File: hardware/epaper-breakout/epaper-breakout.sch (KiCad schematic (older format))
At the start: 68 parts, among them J1 XF2M-3315-1A, J2 C10418, J3 Conn_02x06_Counter_Clockwise, J4 ED060SC4, Q1 IRLML6402, U1 MCP1700-3302E_SOT23, U2 LT1945, U3 LT1945, U5 ESP32-WROVER, U6 CH330N, U7 LM358, U8 74HC4094-normal, U9 MCP9700AT-ETT

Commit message: v5: use ch340g with auto-reset
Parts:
- removed BOOT1: SW2, epaper-breakout:SW_TS-1187A, symbol Switch:SW_Push
- removed C16: 1nF, Capacitor_SMD:C_0603_1608Metric, symbol Device:C
- removed R11, R12: 470, Resistor_SMD:R_0805_2012Metric, symbol Device:R
- removed RESET1: SW1, epaper-breakout:SW_TS-1187A, symbol Switch:SW_Push
- removed U6: CH330N, Package_SO:SOIC-8_3.9x4.9mm_P1.27mm, symbol Interface_USB:CH330N
- added C?: 0.1uF, Capacitor_SMD:C_0603_1608Metric, symbol Device:C
- added Q? (x2): MBT3904DW1, Package_TO_SOT_SMD:SOT-363_SC-70-6, symbol Transistor_BJT:MBT3904DW1
- added R? (x2): 10k, Resistor_SMD:R_0805_2012Metric, symbol Device:R
- added U?: CH340G, Package_SO:SOIC-16_3.9x9.9mm_P1.27mm, symbol Interface_USB:CH340G
- added Y?: Crystal_GND2, symbol Device:Crystal_GND2
- C13, C14: value 0.1uF -> 10pF
- C15: value 1nF -> 0.1uF
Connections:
- net labels added: ~DTR, ~RTS
- wire segments 357 -> 373
- no-connect marks 19 -> 23
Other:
- note added: "Auto-Reset\n"
- moved on the sheet: C1, C10, C11, C12, C13, C14, C15, C19, C2, C20, C3, C4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

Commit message: xc5 connector, power management
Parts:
- removed Q1: IRLML6402, Package_TO_SOT_SMD:SOT-23, symbol Transistor_FET:IRLML6402
- removed Q? (x2): MBT3904DW1, Package_TO_SOT_SMD:SOT-363_SC-70-6, symbol Transistor_BJT:MBT3904DW1
- added Q1, Q2: AO3400A, Package_TO_SOT_SMD:SOT-23, symbol Transistor_FET:AO3400A
- added Q3, Q4: MMBT3904, Package_TO_SOT_SMD:SOT-23, symbol Transistor_BJT:MMBT3904
- added R12: 10k, Resistor_SMD:R_0805_2012Metric, symbol Device:R
- added U6: ED060XC5, epaper-breakout:X05A20H34G, symbol epd_breakout:ED060XC5
- gave numbers to parts that had none: 5
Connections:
- net labels added: EPD_VDD, SMPS_CTRL, SW_VIN
- net labels removed: EPD_POWER, EP_RL, ~SMPS_CTRL
- wire segments 373 -> 426

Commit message: WIP: partial routing
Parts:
- removed Q1, Q2: AO3400A, Package_TO_SOT_SMD:SOT-23, symbol Transistor_FET:AO3400A
- added Q1, Q6: MMBT3904, Package_TO_SOT_SMD:SOT-23, symbol Transistor_BJT:MMBT3904
- added Q2, Q5: AO3401A, Package_TO_SOT_SMD:SOT-23, symbol Transistor_FET:AO3401A
- added R20, R21: 10k, Resistor_SMD:R_0805_2012Metric, symbol Device:R
- added U10: ED060SC7, epaper-breakout:AXT334124, symbol epd_breakout:ED060SC7
- Q3, Q4: LCSC (none) -> C20526
- R12: value 10k -> 1k
- U4: LCSC (none) -> C14267
- Y1: footprint (none) -> Crystal:Crystal_SMD_3225-4Pin_3.2x2.5mm_HandSoldering; LCSC (none) -> C9002
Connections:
- wire segments 426 -> 463
- no-connect marks 23 -> 27
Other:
- moved on the sheet: H1, H2, H3, J1, J3, U9

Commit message: partial routing
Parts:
- removed Q1: MMBT3904, Package_TO_SOT_SMD:SOT-23, symbol Transistor_BJT:MMBT3904
- removed R2, R21, R3, R8, R9: 10k, Resistor_SMD:R_0805_2012Metric, symbol Device:R
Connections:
- net +3.3V: now also R15.1; no longer R15.2
- net EP_CKH: now also U5.23 (IO15); no longer U5.29 (IO5)
- net EP_CKV: now also U5.11 (IO26); no longer U5.10 (IO25)
- net EP_D0: now also Q4.3 (C), R15.2, U5.25 (IO0); no longer U5.9 (IO33_XTAL_32K_N)
- net EP_D1: now also U5.26 (IO4); no longer U5.8 (IO32_XTAL_32K_P)
- net EP_D2: now also U5.29 (IO5); no longer U5.26 (IO4)
- net EP_D3: now also U5.30 (IO18); no longer Q4.3 (C), R15.1, U5.25 (IO0)
- net EP_D4: now also U5.31 (IO19); no longer R13.1, U5.24 (IO2)
- net EP_D5: now also U5.33 (IO21); no longer U5.12 (IO27)
- net EP_D6: now also U5.36 (IO22); no longer U5.33 (IO21)
- net EP_D7: now also U5.37 (IO23); no longer U5.36 (IO22)
- net EP_LE: now also R13.1, U5.24 (IO2); no longer U5.23 (IO15)
- net EP_STH: now also U5.12 (IO27); no longer U5.11 (IO26)
- net at U8.3 (CP): now also U5.8 (IO32_XTAL_32K_P); no longer U5.30 (IO18)
- net at U8.1 (STROBE): now also U5.10 (IO25); no longer U5.31 (IO19)
- net at U8.2 (DATA): now also U5.9 (IO33_XTAL_32K_N); no longer U5.37 (IO23)
- net at Q2.1 (G), Q6.3 (C), R20.1: now also Q5.1 (G)
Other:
- moved on the sheet: Q5, Q6, R12, R15, U8

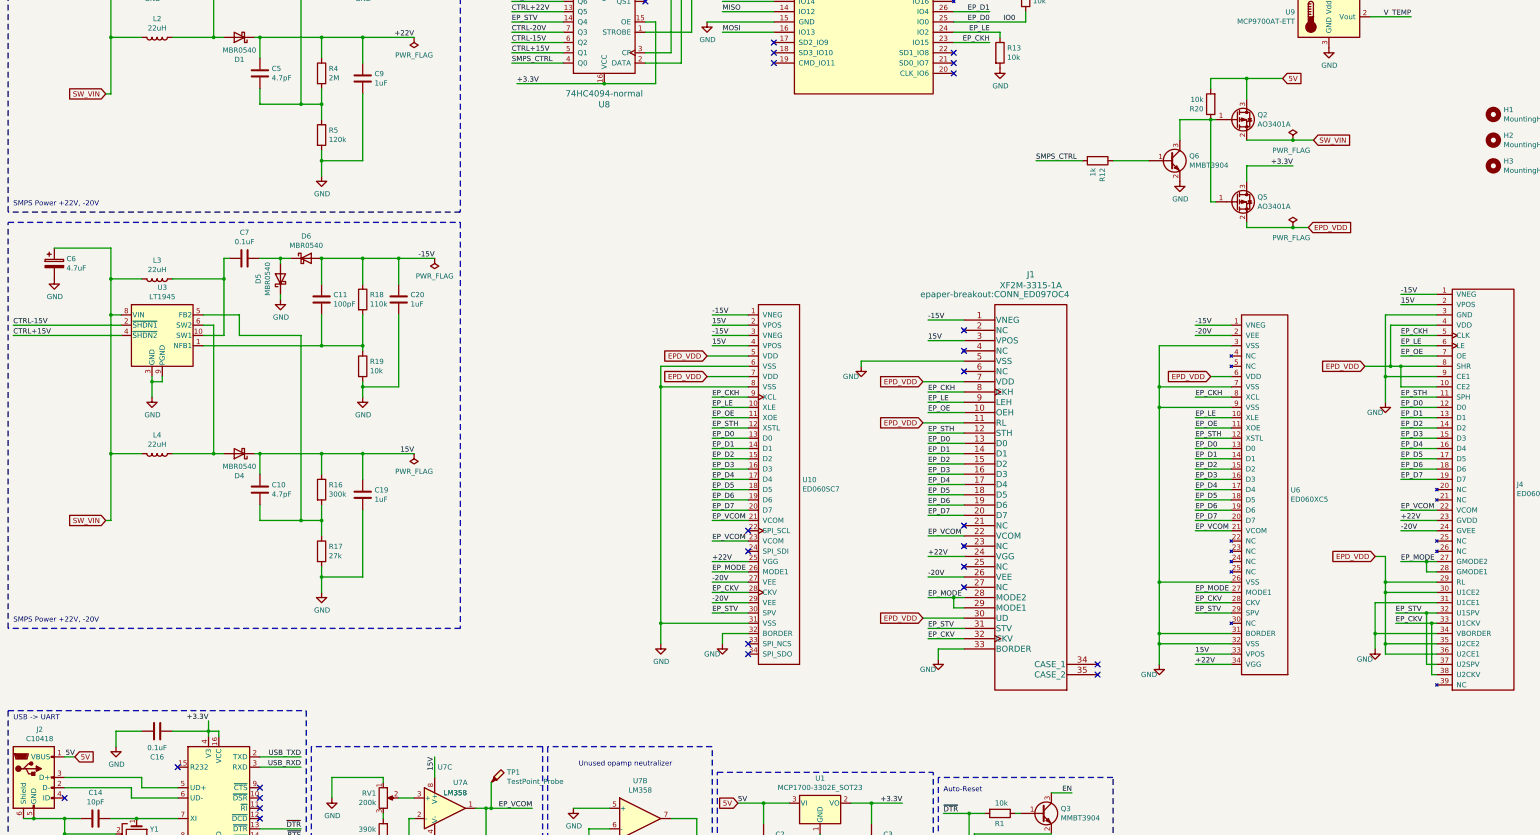
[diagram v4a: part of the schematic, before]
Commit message: v5: lipo charger circuit
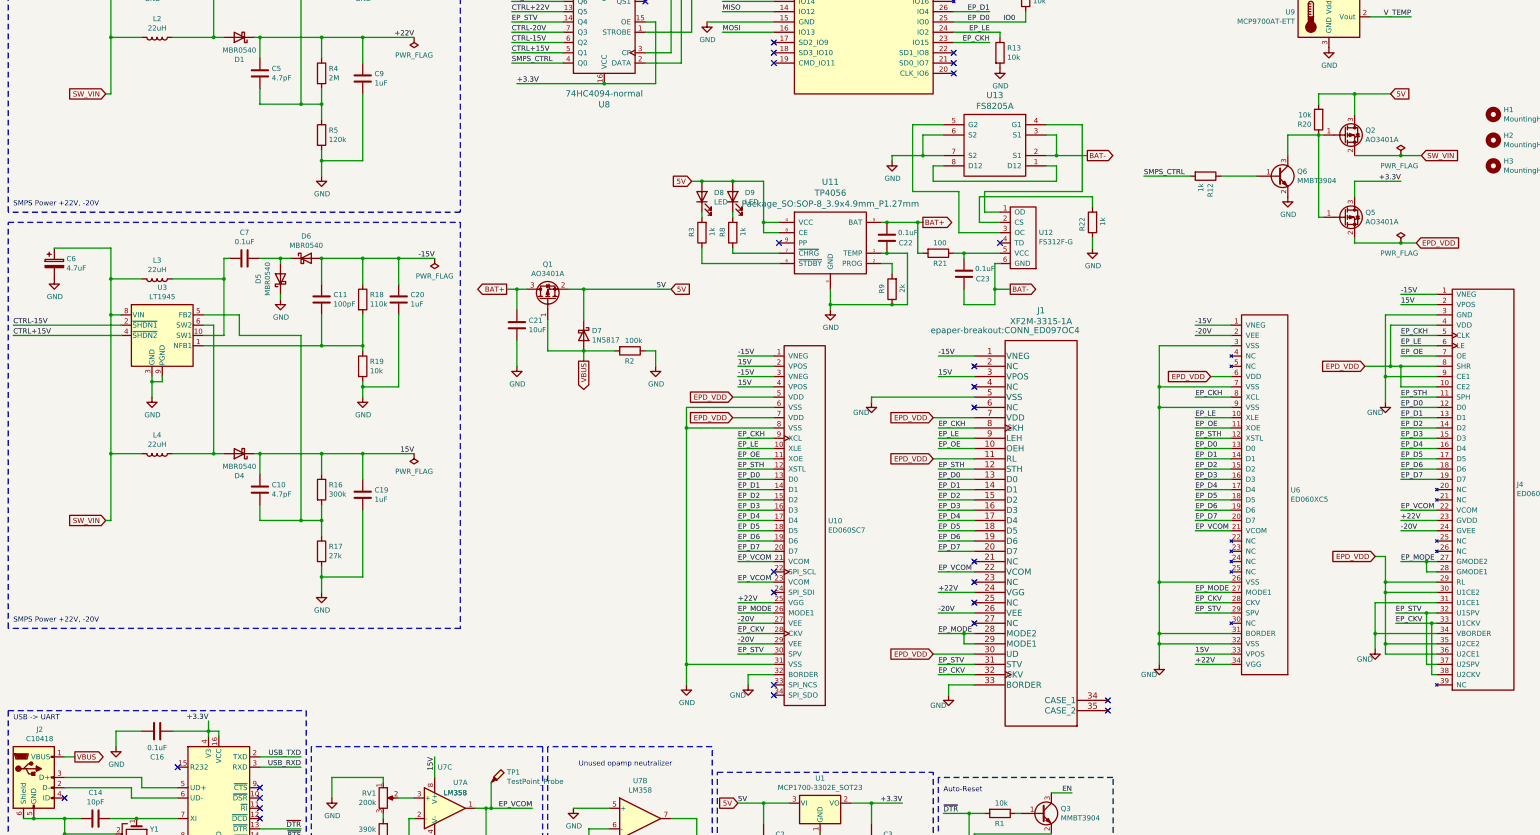
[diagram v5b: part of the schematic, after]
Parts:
- added C21: 10uF, Capacitor_SMD:C_0603_1608Metric, symbol Device:C
- added C22, C23: 0.1uF, Capacitor_SMD:C_0603_1608Metric, symbol Device:C
- added D7: 1N5817, Diode_THT:D_DO-41_SOD81_P10.16mm_Horizontal, symbol Diode:1N5817
- added D8, D9: LED, symbol Device:LED
- added Q1: AO3401A, Package_TO_SOT_SMD:SOT-23, symbol Transistor_FET:AO3401A
- added R2: 100k, Resistor_SMD:R_0805_2012Metric, symbol Device:R
- added R21: 100, Resistor_SMD:R_0805_2012Metric, symbol Device:R
- added R22, R3, R8: 1k, Resistor_SMD:R_0805_2012Metric, symbol Device:R
- added R9: 2k, Resistor_SMD:R_0805_2012Metric, symbol Device:R
- added U11: TP4056, Package_SO:SOP-8_3.9x4.9mm_P1.27mm, symbol tp4056:TP4056
- added U12: FS312F-G, Package_TO_SOT_SMD:SOT-23-6, symbol epd_breakout:FS312F-G
- added U13: FS8205A, Package_SO:TSSOP-8_4.4x3mm_P0.65mm, symbol fs8205a:FS8205A
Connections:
- net 5V: now also D7.1 (K), D8.2 (A), D9.2 (A), Q1.2 (S), U11.4 (VCC), U11.8 (CE); no longer J2.1 (VBUS)
- net GND: now also C21.2, C22.1, R2.1, R22.1, R9.1, U11.1 (TEMP), U11.3 (GND), U13.6 (S2), U13.7 (S2)
- new net: R8.1, U11.7 (~CHRG)
- new net: D9.1 (K), R8.2
- new net: R9.2, U11.2 (PROG)
- new net: R3.1, U11.6 (~STDBY)
- new net: U13.1 (D12), U13.8 (D12)
- new net: U12.1 (OD), U13.4 (G1)
- new net: U12.3 (OC), U13.5 (G2)
- new net: D8.1 (K), R3.2
- new net: R22.2, U12.2 (CS)
- new net: C23.2, R21.1, U12.5 (VCC)
- new net BAT+: C21.1, C22.2, Q1.3 (D), R21.2, U11.5 (BAT)
- new net BAT-: C23.1, U12.6 (GND), U13.2 (S1), U13.3 (S1)
- new net VBUS: D7.2 (A), J2.1 (VBUS), Q1.1 (G), R2.2
- no-connect marks 27 -> 29
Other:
- moved on the sheet: J1, Q2, Q5, Q6, R12, R20, U10

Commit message: v5 fix pin functions
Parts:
- D8: value LED -> LED GREEN; footprint (none) -> LED_SMD:LED_0805_2012Metric
- D9: value LED -> LED RED; footprint (none) -> LED_SMD:LED_0805_2012Metric
- U11: footprint Package_SO:SOP-8_3.9x4.9mm_P1.27mm -> epaper-breakout:TP4056_SOP-8-PP
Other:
- moved on the sheet: J1, J4, U10, U6

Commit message: more routing
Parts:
- added J?: Conn_01x02_Male, Connector_PinHeader_2.54mm:PinHeader_1x02_P2.54mm_Vertical, symbol Connector:Conn_01x02_Male
- D7: footprint Diode_THT:D_DO-41_SOD81_P10.16mm_Horizontal -> Diode_SMD:D_SOD-123
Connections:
- net BAT+: now also J?.1 (Pin_1)
- net BAT-: now also J?.2 (Pin_2)
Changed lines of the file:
@@
 F 0 "D7" V 6104 5830 50  0000 L CNN
 F 1 "1N5817" V 6195 5830 50  0000 L CNN
-F 2 "Diode_THT:D_DO-41_SOD81_P10.16mm_Horizontal" H 6150 5575 50  0001 C CNN
+F 2 "Diode_SMD:D_SOD-123" H 6150 5575 50  0001 C CNN
 F 3 "http://www.vishay.com/docs/88525/1n5817.pdf" H 6150 5750 50  0001 C CNN
 	1    6150 5750
@@
 Wire Wire Line
 	7600 4250 7900 4250
+$Comp
+L Connector:Conn_01x02_Male J?
+U 1 1 655CB8A7
+P 5750 6750
+F 0 "J?" H 5858 6931 50  0000 C CNN
+F 1 "Conn_01x02_Male" H 5858 6840 50  0000 C CNN
+F 2 "Connector_PinHeader_2.54mm:PinHeader_1x02_P2.54mm_Vertical" H 5750 6750 50  0001 C CNN
+F 3 "~" H 5750 6750 50  0001 C CNN
+	1    5750 6750
+	1    0    0    -1
+$EndComp
+Text GLabel 6100 6750 2    50   Input ~ 0
+BAT+
+Text GLabel 6100 6850 2    50   Input ~ 0
+BAT-
+Wire Wire Line
+	5950 6750 6100 6750
+Wire Wire Line
+	6100 6850 5950 6850
 $EndSCHEMATC

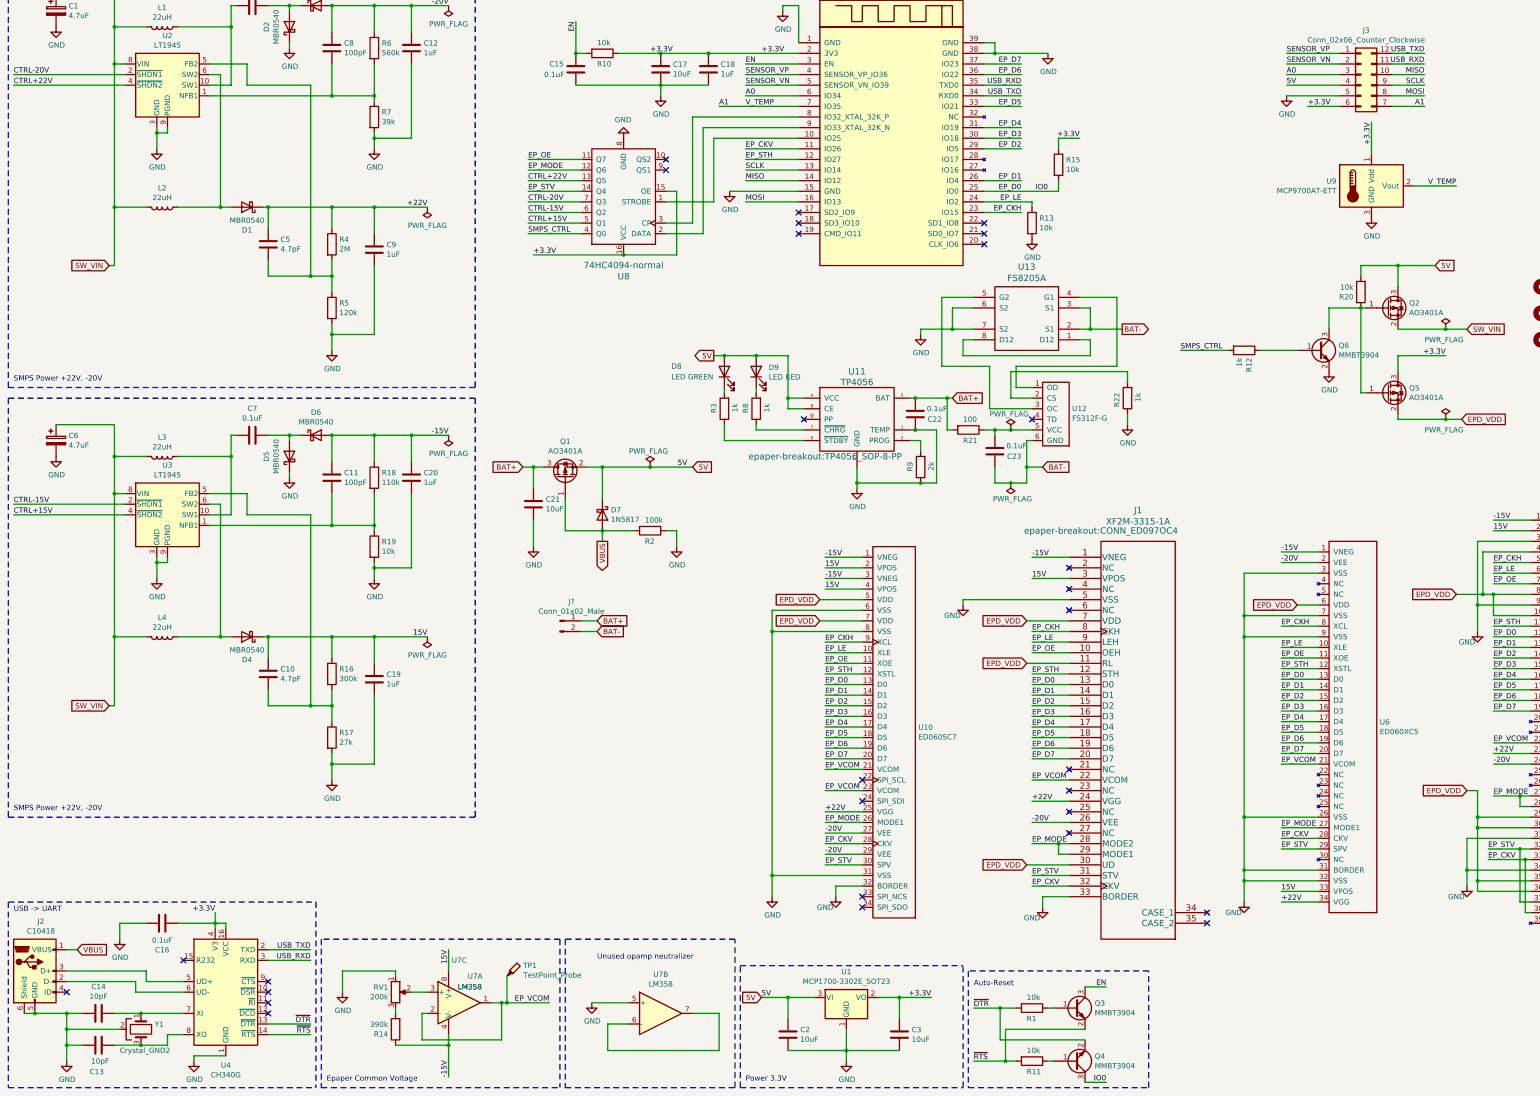
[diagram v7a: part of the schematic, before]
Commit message: remove battery protection, simplify
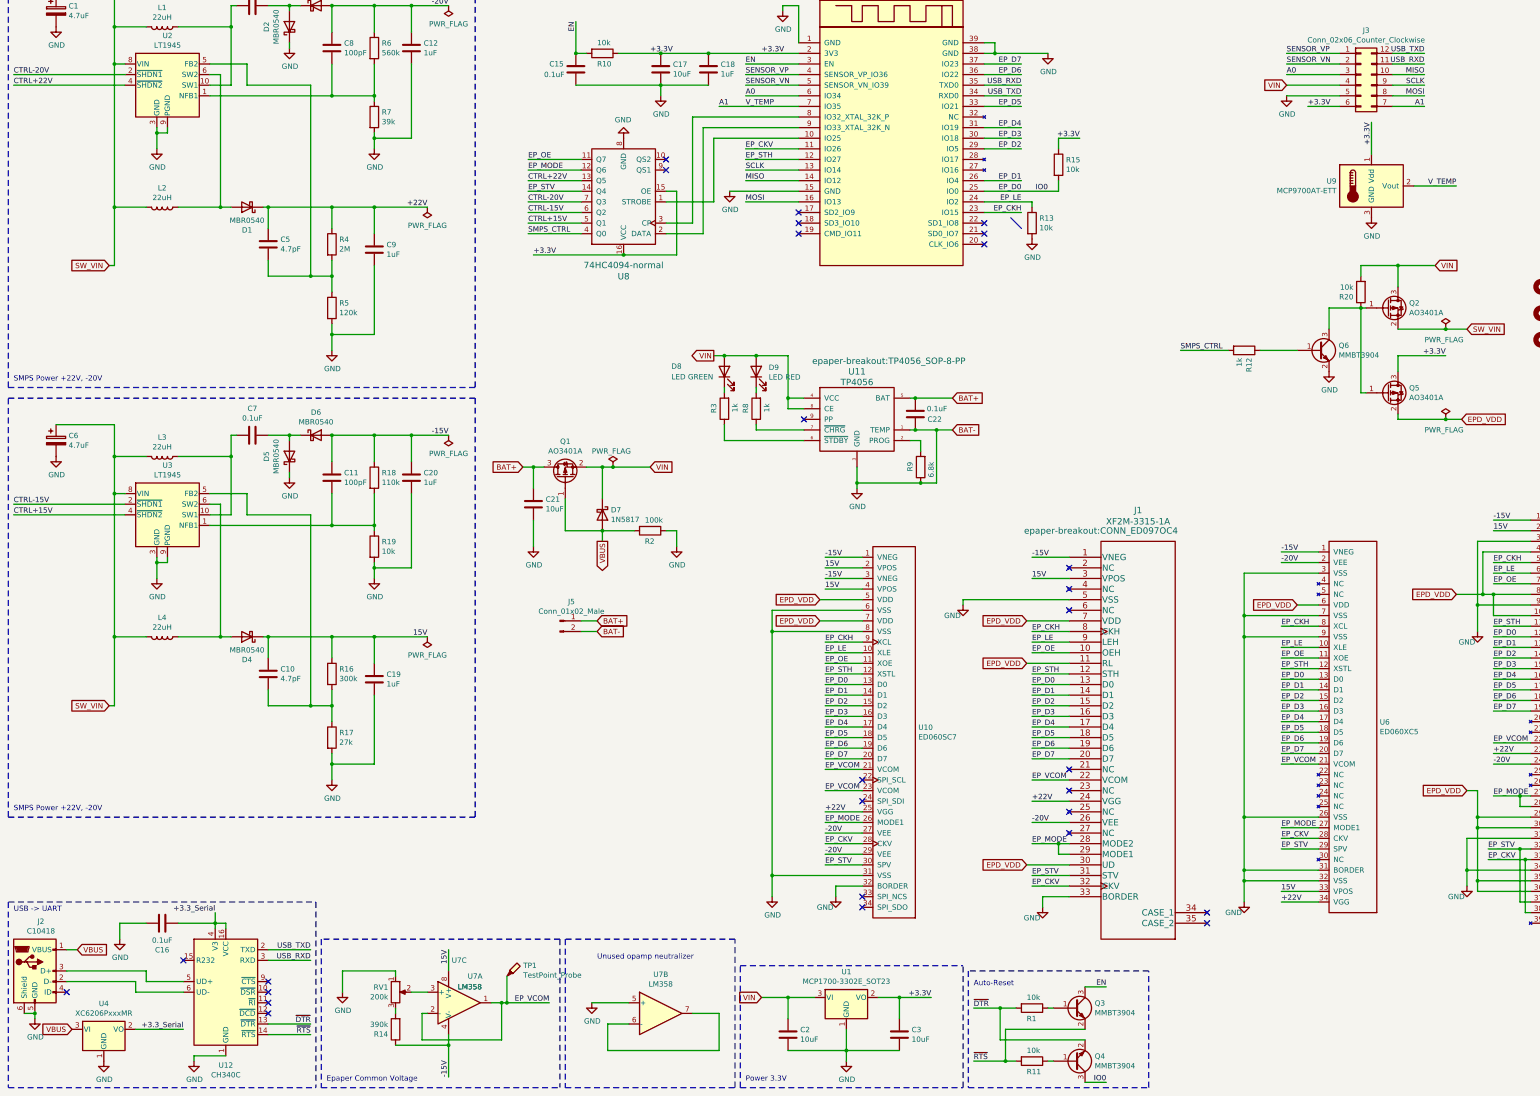
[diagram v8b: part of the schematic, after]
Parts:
- removed C13, C14: 10pF, Capacitor_SMD:C_0603_1608Metric, symbol Device:C
- removed C23: 0.1uF, Capacitor_SMD:C_0603_1608Metric, symbol Device:C
- removed R21: 100, Resistor_SMD:R_0805_2012Metric, symbol Device:R
- removed R22: 1k, Resistor_SMD:R_0805_2012Metric, symbol Device:R
- removed U12: FS312F-G, Package_TO_SOT_SMD:SOT-23-6, symbol epd_breakout:FS312F-G
- removed U13: FS8205A, Package_SO:TSSOP-8_4.4x3mm_P0.65mm, symbol fs8205a:FS8205A
- removed U4: CH340G, Package_SO:SOIC-16_3.9x9.9mm_P1.27mm, symbol Interface_USB:CH340G
- removed Y1: Crystal_GND2, Crystal:Crystal_SMD_3225-4Pin_3.2x2.5mm_HandSoldering, symbol Device:Crystal_GND2
- added U12: CH340C, Package_SO:SOIC-16_3.9x9.9mm_P1.27mm, symbol Interface_USB:CH340C
- added U4: XC6206PxxxMR, Package_TO_SOT_SMD:SOT-23, symbol Regulator_Linear:XC6206PxxxMR
- C22: LCSC C1588 -> C14663
- D7: LCSC (none) -> C8598
- L1, L2, L3, L4: LCSC C326331 -> C206321
- Q1: LCSC (none) -> C15127
- R2: LCSC (none) -> C17407
- R3, R8: LCSC (none) -> C17513
- R9: value 2k -> 6.8k; LCSC (none) -> C17772
- gave numbers to parts that had none: 1
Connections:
- net BAT- is gone; now on net GND: J5.2 (Pin_2)
- net +3.3V: no longer C16.1
- net GND: now also U12.1 (GND), U4.1 (GND)
- net USB_RXD: now also U12.3 (RXD)
- net USB_TXD: now also U12.2 (TXD)
- net VBUS: now also U4.3 (VI)
- net ~DTR: now also U12.13 (~DTR)
- net ~RTS: now also U12.14 (~RTS)
- net at J2.2 (D-): now also U12.6 (UD-)
- net at J2.3 (D+): now also U12.5 (UD+)
- net 5V renamed VIN
- new net +3.3_Serial: C16.1, U12.16 (VCC), U12.4 (V3), U4.2 (VO)
- no-connect marks 29 -> 28
